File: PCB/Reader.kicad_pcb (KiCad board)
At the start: 2 copper layers, 40.4 x 60 mm, 42 parts, among them J1 Conn_01x04, J2 Amphenol Dubox ‎76383-402LF‎, J3 Conn_01x04, J4 Conn_01x08, J5 Conn_01x10, J6 Conn_01x03, J7 Conn_01x02, Q1 2N7002, Q2 2N7002, Q3 2N7002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

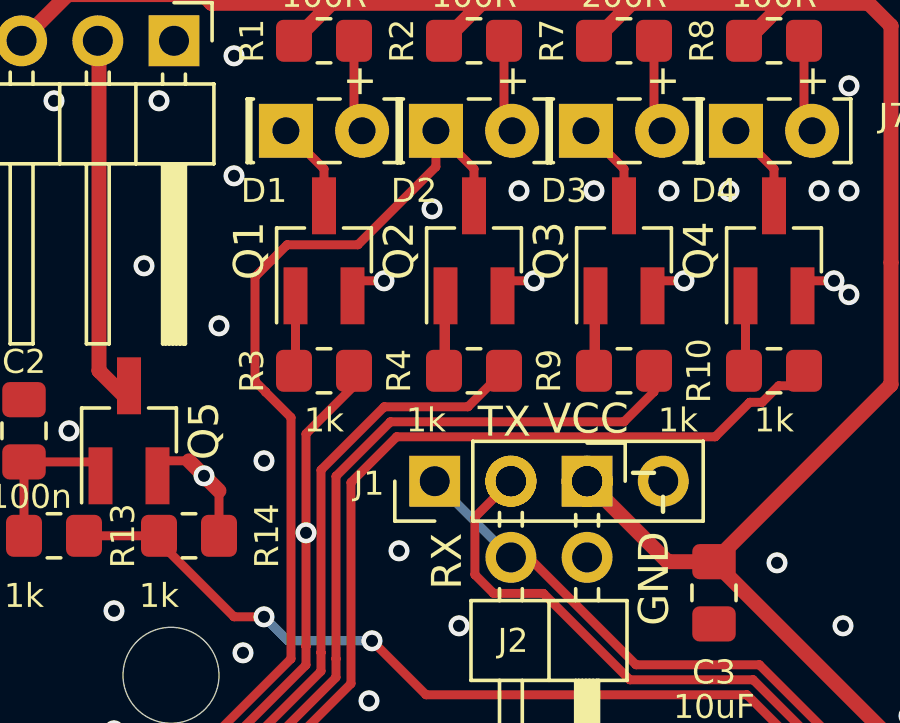
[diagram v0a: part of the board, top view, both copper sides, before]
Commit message: DRC: (Re)move two vias
Seems tracks were moved over/near these vias, producing a short and
clearance failure. This removes one via and moves the other.
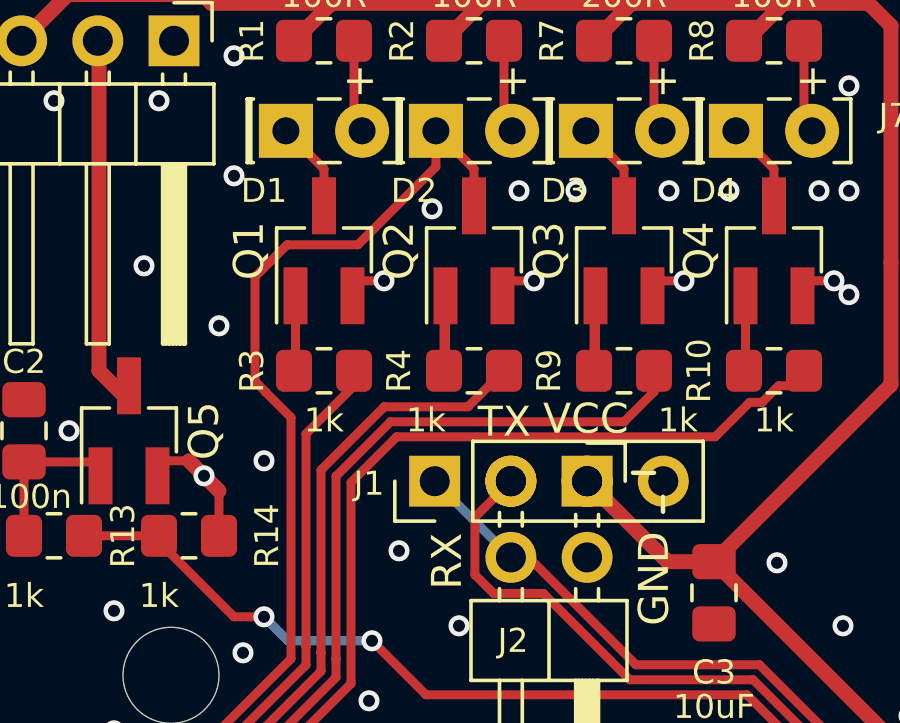
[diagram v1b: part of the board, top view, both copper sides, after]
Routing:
- net GND: vias 189 -> 188
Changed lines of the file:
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@@
 	)
 	(via
-		(at 101.5 70)
+		(at 100.9 69.99)
 		(size 0.7)
 		(drill 0.4)
@@
 		(size 0.7)
 		(drill 0.4)
-		(layers "F.Cu" "B.Cu")
-		(net 1)
-	)
-	(via
-		(at 91.9 81.4)
-		(size 0.7)
-		(drill 0.4)
